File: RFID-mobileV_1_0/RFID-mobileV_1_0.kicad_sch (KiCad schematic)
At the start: 52 parts, among them J1 USB_C_Receptacle_USB2.0, Q1 MMBT3904, SW1 SW_Push, U1 XC6206P332MR, U2 E22-400T22S, U3 STM32G030FxP, U4 LM321, U5 TP4054

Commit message: update
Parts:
- BT1: value Battery -> (none); footprint Connector_Molex:Molex_KK-254_AE-6410-02A_1x02_P2.54mm_Vertical -> (none); now left out of the parts list
- C5: value C -> (none); footprint Capacitor_SMD:C_0805_2012Metric -> (none)
- U2: value E22-400T22S -> (none); footprint RF_Module:E220-400TxxS -> (none); now left out of the parts list
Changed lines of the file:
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@@
   )
   (symbol (lib_id "Device:Battery") (at 173.99 100.965 0) (unit 1)
-    (in_bom yes) (on_board yes) (fields_autoplaced)
+    (in_bom no) (on_board no) (fields_autoplaced)
     (property "Reference" "BT1" (id 0) (at 177.165 99.3139 0)
       (effects (font (size 1.27 1.27)) (justify left))
     )
-    (property "Value" "Battery" (id 1) (at 177.165 101.8539 0)
-      (effects (font (size 1.27 1.27)) (justify left))
-    )
-    (property "Footprint" "Connector_Molex:Molex_KK-254_AE-6410-02A_1x02_P2.54mm_Vertical" (id 2) (at 173.99 99.441 90)
+    (property "Value" "" (id 1) (at 177.165 101.8539 0)
+      (effects (font (size 1.27 1.27)) (justify left))
+    )
+    (property "Footprint" "" (id 2) (at 173.99 99.441 90)
       (effects (font (size 1.27 1.27)) hide)
     )
@@
   )
   (symbol (lib_id "RF_Module:E220-400TxxS") (at 90.805 154.94 0) (unit 1)
-    (in_bom yes) (on_board yes)
+    (in_bom no) (on_board yes)
     (property "Reference" "U2" (id 0) (at 90.17 133.985 0))
-    (property "Value" "E22-400T22S" (id 1) (at 90.17 136.525 0))
-    (property "Footprint" "RF_Module:E220-400TxxS" (id 2) (at 90.17 139.065 0)
+    (property "Value" "" (id 1) (at 90.17 136.525 0))
+    (property "Footprint" "" (id 2) (at 90.17 139.065 0)
       (effects (font (size 1.27 1.27)) hide)
     )
@@
       (effects (font (size 1.27 1.27)) (justify left))
     )
-    (property "Value" "C" (id 1) (at 161.29 46.3549 0)
-      (effects (font (size 1.27 1.27)) (justify left))
-    )
-    (property "Footprint" "Capacitor_SMD:C_0805_2012Metric" (id 2) (at 158.4452 48.895 0)
+    (property "Value" "" (id 1) (at 161.29 46.3549 0)
+      (effects (font (size 1.27 1.27)) (justify left))
+    )
+    (property "Footprint" "" (id 2) (at 158.4452 48.895 0)
       (effects (font (size 1.27 1.27)) hide)
     )
@@
     )
     (path "/600d1817-b711-4dc4-847d-e60b9198af7b"
-      (reference "C5") (unit 1) (value "C") (footprint "Capacitor_SMD:C_0805_2012Metric")
+      (reference "C5") (unit 1) (value "0.1uF") (footprint "Capacitor_SMD:C_0805_2012Metric")
     )
     (path "/d5f34cdc-c982-4ea2-9952-8b32c1792e7d"

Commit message: fix BT1
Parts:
- C5: value (none) -> 0.1uF; footprint (none) -> Capacitor_SMD:C_0805_2012Metric
- J2, J4: value (none) -> Conn_01x05_Male; footprint (none) -> Connector_PinHeader_2.54mm:PinHeader_1x05_P2.54mm_Vertical
- J3: value (none) -> Conn_01x05_Female; footprint (none) -> Connector_PinHeader_2.54mm:PinHeader_1x05_P2.54mm_Vertical
- U2: value (none) -> E22-400T22S; footprint (none) -> RF_Module:E220-400TxxS
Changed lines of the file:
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@@
     (in_bom no) (on_board yes) (fields_autoplaced)
     (property "Reference" "J2" (id 0) (at 30.48 149.86 0))
-    (property "Value" "" (id 1) (at 30.48 152.4 0))
-    (property "Footprint" "" (id 2) (at 29.845 160.655 0)
+    (property "Value" "Conn_01x05_Male" (id 1) (at 30.48 152.4 0))
+    (property "Footprint" "Connector_PinHeader_2.54mm:PinHeader_1x05_P2.54mm_Vertical" (id 2) (at 29.845 160.655 0)
       (effects (font (size 1.27 1.27)) hide)
     )
@@
   )
   (symbol (lib_id "Device:Battery") (at 173.99 100.965 0) (unit 1)
-    (in_bom no) (on_board no) (fields_autoplaced)
+    (in_bom no) (on_board yes) (fields_autoplaced)
     (property "Reference" "BT1" (id 0) (at 177.165 99.3139 0)
       (effects (font (size 1.27 1.27)) (justify left))
@@
     (in_bom no) (on_board yes)
     (property "Reference" "J4" (id 0) (at 254 20.955 0))
-    (property "Value" "" (id 1) (at 259.08 40.005 0))
-    (property "Footprint" "" (id 2) (at 250.825 29.21 0)
+    (property "Value" "Conn_01x05_Male" (id 1) (at 259.08 40.005 0))
+    (property "Footprint" "Connector_PinHeader_2.54mm:PinHeader_1x05_P2.54mm_Vertical" (id 2) (at 250.825 29.21 0)
       (effects (font (size 1.27 1.27)) hide)
     )
@@
     (in_bom no) (on_board yes)
     (property "Reference" "U2" (id 0) (at 90.17 133.985 0))
-    (property "Value" "" (id 1) (at 90.17 136.525 0))
-    (property "Footprint" "" (id 2) (at 90.17 139.065 0)
+    (property "Value" "E22-400T22S" (id 1) (at 90.17 136.525 0))
+    (property "Footprint" "RF_Module:E220-400TxxS" (id 2) (at 90.17 139.065 0)
       (effects (font (size 1.27 1.27)) hide)
     )
@@
       (effects (font (size 1.27 1.27)) (justify left))
     )
-    (property "Value" "" (id 1) (at 161.29 46.3549 0)
-      (effects (font (size 1.27 1.27)) (justify left))
-    )
-    (property "Footprint" "" (id 2) (at 158.4452 48.895 0)
+    (property "Value" "0.1uF" (id 1) (at 161.29 46.3549 0)
+      (effects (font (size 1.27 1.27)) (justify left))
+    )
+    (property "Footprint" "Capacitor_SMD:C_0805_2012Metric" (id 2) (at 158.4452 48.895 0)
       (effects (font (size 1.27 1.27)) hide)
     )
@@
       (effects (font (size 1.27 1.27)) (justify left))
     )
-    (property "Value" "" (id 1) (at 203.835 45.085 0)
-      (effects (font (size 1.27 1.27)) (justify left))
-    )
-    (property "Footprint" "" (id 2) (at 217.805 38.1 0)
-      (effects (font (size 1.27 1.27)) hide)
-    )
+    (property "Value" "Conn_01x05_Female" (id 1) (at 203.835 45.085 0)
+      (effects (font (size 1.27 1.27)) (justify left))
+    )
+    (property "Footprint" "Connector_PinHeader_2.54mm:PinHeader_1x05_P2.54mm_Vertical" (id 2) (at 217.805 38.1 0)
+      (effects (font (size 1.27 1.27)) hide)
+    )

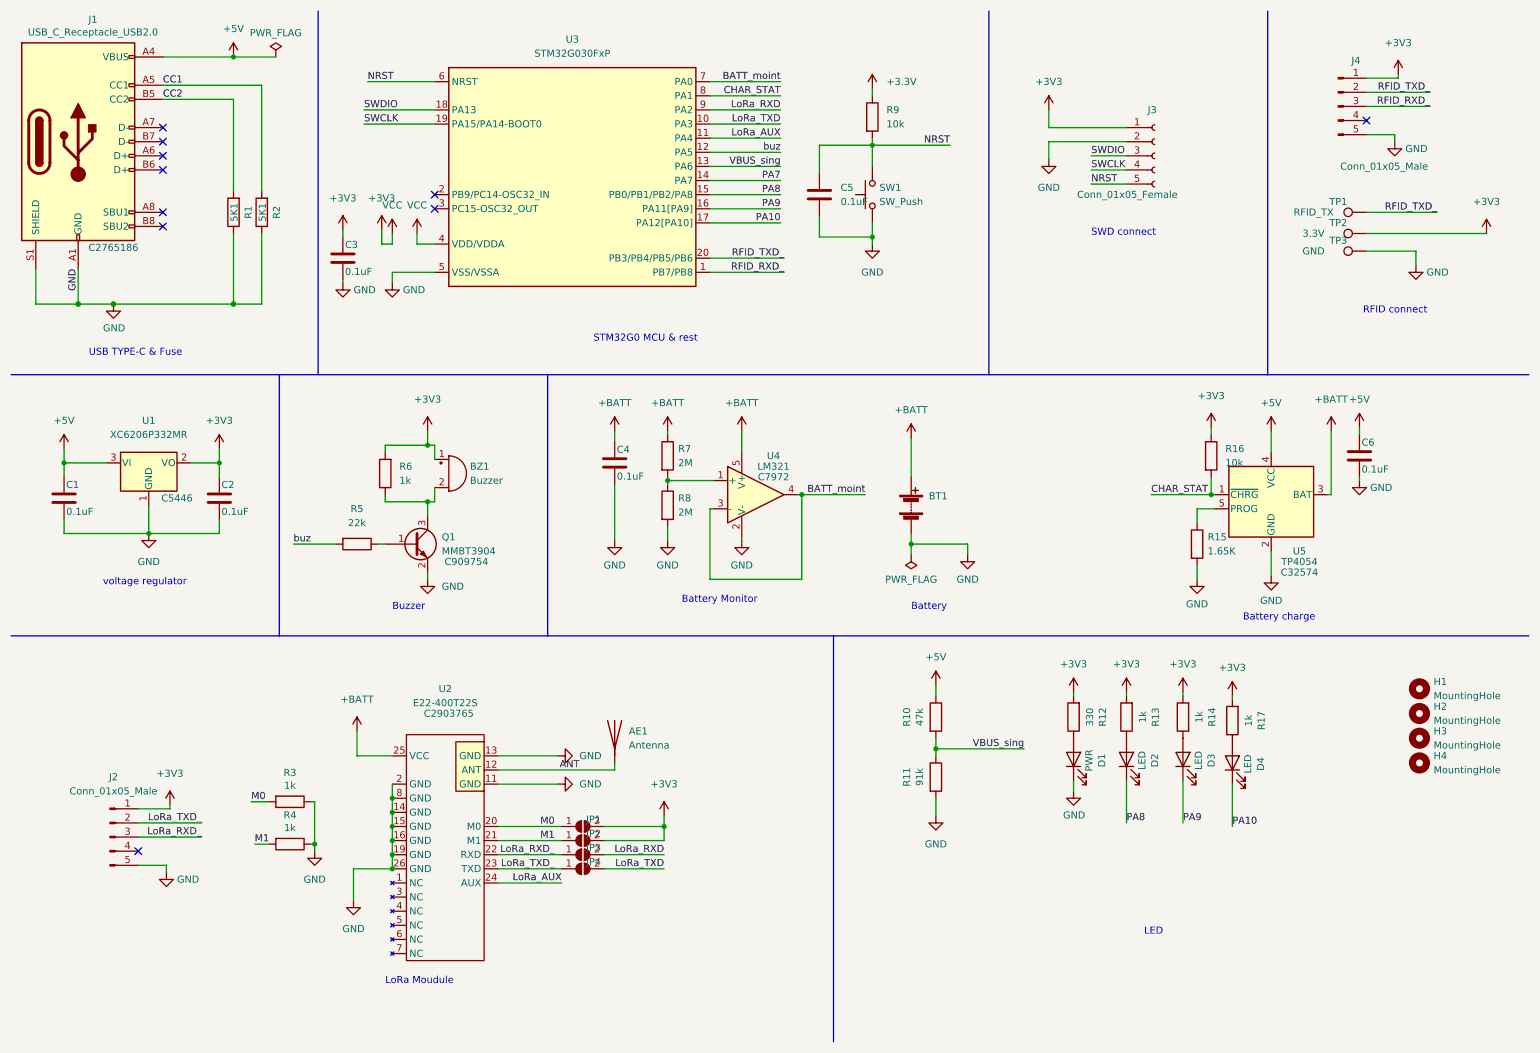
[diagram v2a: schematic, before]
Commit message: Update RFID-mobileV_1_0.kicad_sch
V2.RFID 通信腳位使用錯誤(TX RX 交換)。
V3.電源3.3V 應由電池端供電，不能由5V 供電。
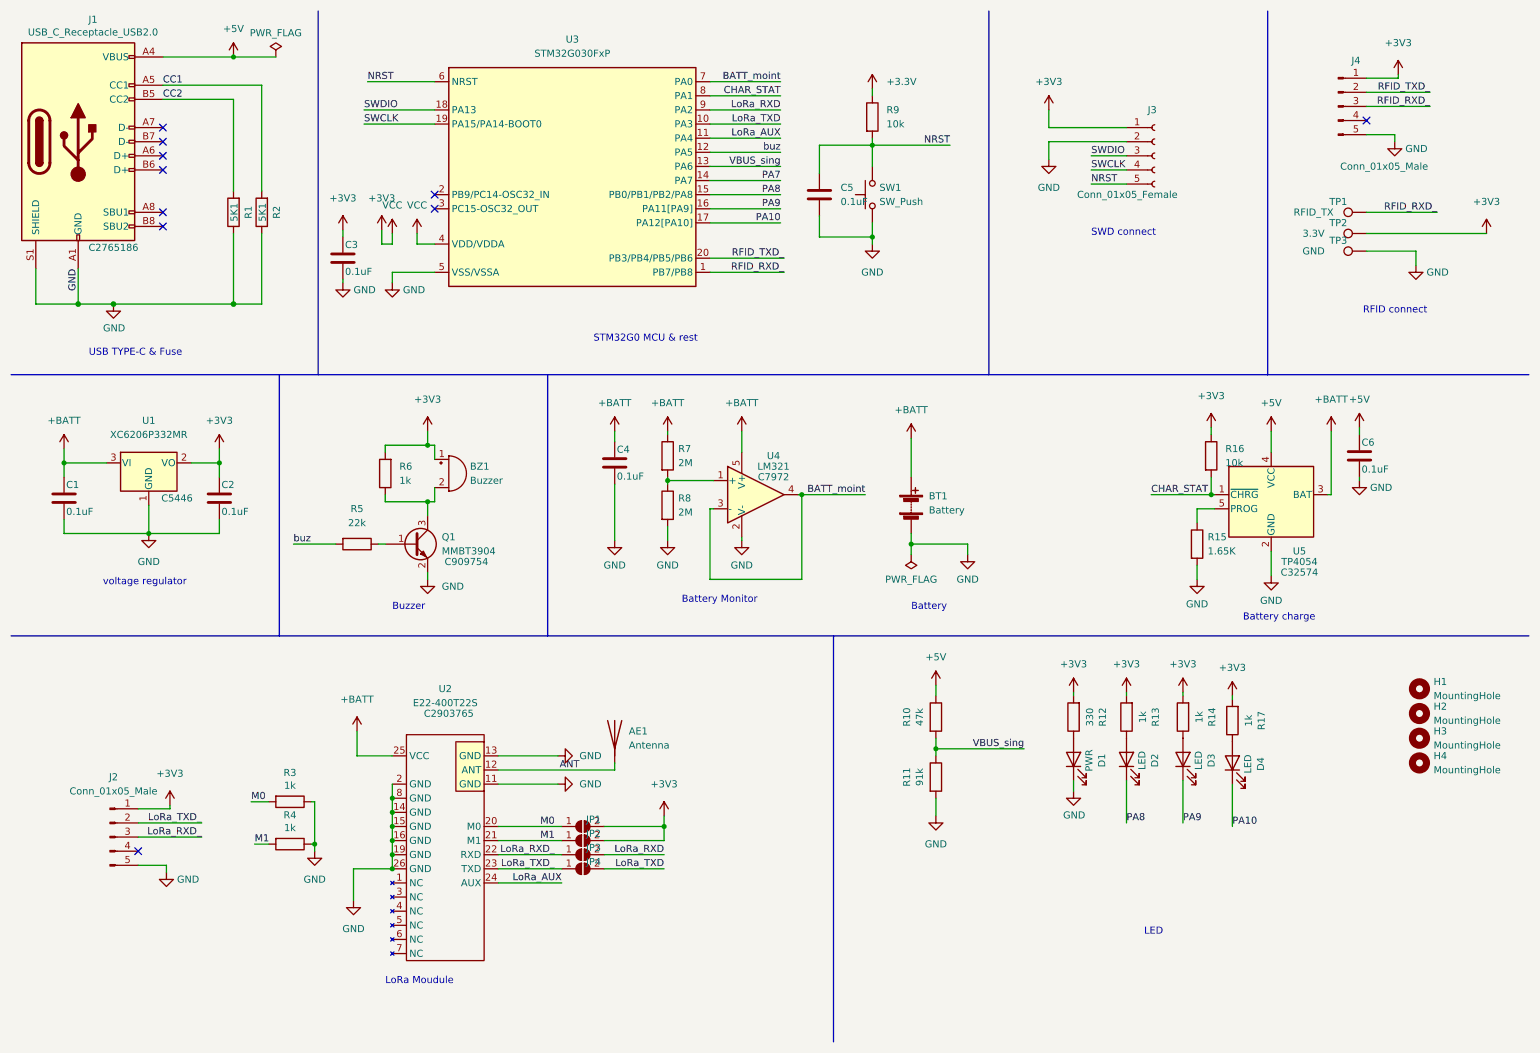
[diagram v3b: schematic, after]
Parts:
- BT1: value (none) -> Battery; footprint (none) -> Connector_Molex:Molex_KK-254_AE-6410-02A_1x02_P2.54mm_Vertical
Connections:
- net +5V: no longer C1.1, U1.3 (VI)
- net +BATT: now also C1.1, U1.3 (VI)
- net RFID_RXD_: now also TP1.1
- net RFID_TXD_: no longer TP1.1
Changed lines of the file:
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@@
     (effects (font (size 1.27 1.27)) (justify right bottom))
   )
-  (label "RFID_TXD_" (at 268.605 48.26 180)
+  (label "RFID_RXD_" (at 268.605 48.26 180)
     (effects (font (size 1.27 1.27)) (justify right bottom))
   )
@@
     (pin "1")
   )
+  (symbol (lib_id "power:+BATT") (at 21.59 90.805 0) (unit 1)
+    (in_bom yes) (on_board yes) (fields_autoplaced)
+    (property "Reference" "#PWR?" (id 0) (at 21.59 94.615 0)
+      (effects (font (size 1.27 1.27)) hide)
+    )
+    (property "Value" "+BATT" (id 1) (at 21.59 85.725 0))
+    (property "Footprint" "" (id 2) (at 21.59 90.805 0)
+      (effects (font (size 1.27 1.27)) hide)
+    )
+    (property "Datasheet" "" (id 3) (at 21.59 90.805 0)
+      (effects (font (size 1.27 1.27)) hide)
+    )
+    (pin "1")
+  )
   (symbol (lib_id "power:+3V3") (at 40.64 154.94 0) (unit 1)
     (in_bom yes) (on_board yes) (fields_autoplaced)
@@
       (effects (font (size 1.27 1.27)) (justify left))
     )
-    (property "Value" "" (id 1) (at 177.165 101.8539 0)
-      (effects (font (size 1.27 1.27)) (justify left))
-    )
-    (property "Footprint" "" (id 2) (at 173.99 99.441 90)
+    (property "Value" "Battery" (id 1) (at 177.165 101.8539 0)
+      (effects (font (size 1.27 1.27)) (justify left))
+    )
+    (property "Footprint" "Connector_Molex:Molex_KK-254_AE-6410-02A_1x02_P2.54mm_Vertical" (id 2) (at 173.99 99.441 90)
       (effects (font (size 1.27 1.27)) hide)
     )
@@
     (pin "2")
   )
-  (symbol (lib_id "power:+5V") (at 21.59 90.805 0) (unit 1)
-    (in_bom yes) (on_board yes) (fields_autoplaced)
-    (property "Reference" "#PWR01" (id 0) (at 21.59 94.615 0)
-      (effects (font (size 1.27 1.27)) hide)
-    )
-    (property "Value" "+5V" (id 1) (at 21.59 85.725 0))
-    (property "Footprint" "" (id 2) (at 21.59 90.805 0)
-      (effects (font (size 1.27 1.27)) hide)
-    )
-    (property "Datasheet" "" (id 3) (at 21.59 90.805 0)
-      (effects (font (size 1.27 1.27)) hide)
-    )
-    (pin "1")
-  )
   (symbol (lib_id "power:GND") (at 130.175 107.315 0) (unit 1)
     (in_bom yes) (on_board yes) (fields_autoplaced)
@@
       (reference "#FLG02") (unit 1) (value "PWR_FLAG") (footprint "")
     )
-    (path "/df68d577-4fdb-42a9-a618-f997c5cb205b"
-      (reference "#PWR01") (unit 1) (value "+5V") (footprint "")
-    )
     (path "/cd50b8dc-829d-4a1d-8f2a-6471f378ba87"
       (reference "#PWR02") (unit 1) (value "GND") (footprint "")
@@
       (reference "#PWR051") (unit 1) (value "+3V3") (footprint "")
     )
+    (path "/143a35af-b893-4b64-95e7-41f6c73b6bcb"
+      (reference "#PWR?") (unit 1) (value "+BATT") (footprint "")
+    )
     (path "/ac27cb01-7e08-4126-9053-c19587e4f0b6"
